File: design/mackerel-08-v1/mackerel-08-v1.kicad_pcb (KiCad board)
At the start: 4 copper layers, 160 x 99.1 mm, 40 parts, among them J1 Conn_02x20_Odd_Even, J2 DC_Jack, J3 Conn_02x10_Odd_Even, J4 Conn_02x10_Odd_Even, J5 Conn_01x06, J6 Conn_01x06, SW1 SW_Push, U1 MC68008, U10 XR68C681, U11 74HC595, U12 ATF22V10C, U13 74HC10, U14 ATF22V10C, U15 NE555P, U2 AS7C4096A, U3 AS7C4096A, U4 AS7C4096A, U5 AS7C4096A, U6 AS7C4096A, U7 AS7C4096A, U8 AS7C4096A, U9 SST39SF040, X1 CXO_DIP8, X2 CXO_DIP8

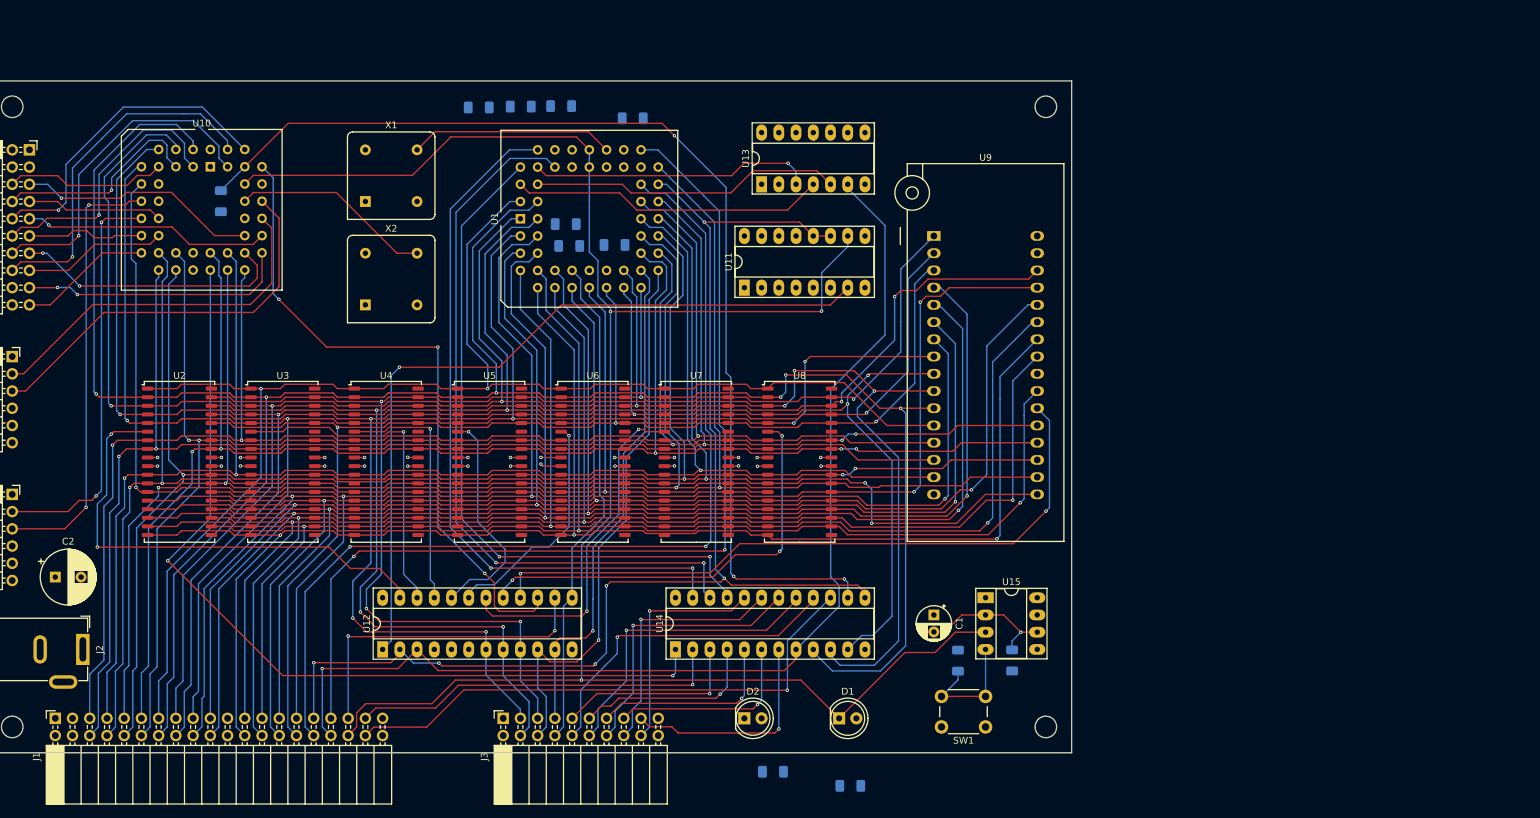
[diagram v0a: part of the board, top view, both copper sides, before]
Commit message: Add decoupling caps
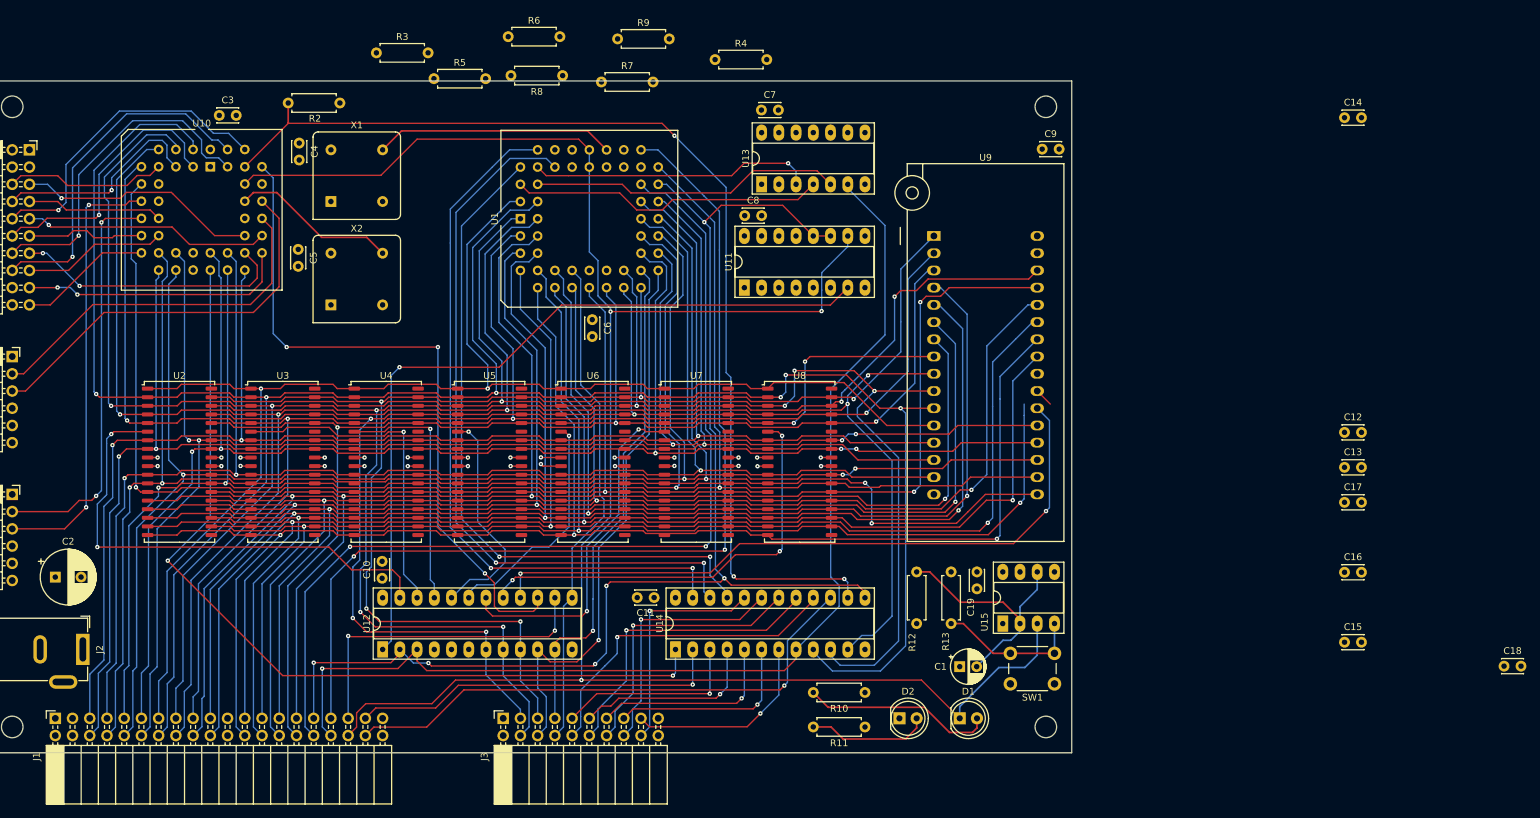
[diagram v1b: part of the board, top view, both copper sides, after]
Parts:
- added C10: C, Capacitor_THT:C_Disc_D3.0mm_W2.0mm_P2.50mm, F.Cu at (78.7, 93.6)
- added C11: C, Capacitor_THT:C_Disc_D3.0mm_W2.0mm_P2.50mm, F.Cu at (118.8, 96.5)
- added C12: C, Capacitor_THT:C_Disc_D3.0mm_W2.0mm_P2.50mm, F.Cu at (220.6, 72.1)
- added C13: C, Capacitor_THT:C_Disc_D3.0mm_W2.0mm_P2.50mm, F.Cu at (220.6, 77.3)
- added C14: C, Capacitor_THT:C_Disc_D3.0mm_W2.0mm_P2.50mm, F.Cu at (220.6, 25.7)
- added C15: C, Capacitor_THT:C_Disc_D3.0mm_W2.0mm_P2.50mm, F.Cu at (220.6, 103.1)
- added C16: C, Capacitor_THT:C_Disc_D3.0mm_W2.0mm_P2.50mm, F.Cu at (220.6, 92.8)
- added C17: C, Capacitor_THT:C_Disc_D3.0mm_W2.0mm_P2.50mm, F.Cu at (220.6, 82.5)
- added C18: C, Capacitor_THT:C_Disc_D3.0mm_W2.0mm_P2.50mm, F.Cu at (244.1, 106.6)
- added C19: C, Capacitor_THT:C_Disc_D3.0mm_W2.0mm_P2.50mm, F.Cu at (166.4, 92.7)
- added C3: C, Capacitor_THT:C_Disc_D3.0mm_W2.0mm_P2.50mm, F.Cu at (54.7, 25.4)
- added C4: C, Capacitor_THT:C_Disc_D3.0mm_W2.0mm_P2.50mm, F.Cu at (66.4, 29.5)
- added C5: C, Capacitor_THT:C_Disc_D3.0mm_W2.0mm_P2.50mm, F.Cu at (66.3, 45.2)
- added C6: C, Capacitor_THT:C_Disc_D3.0mm_W2.0mm_P2.50mm, F.Cu at (109.7, 55.5)
- added C7: C, Capacitor_THT:C_Disc_D3.0mm_W2.0mm_P2.50mm, F.Cu at (134.6, 24.6)
- added C8: C, Capacitor_THT:C_Disc_D3.0mm_W2.0mm_P2.50mm, F.Cu at (132.1, 40.2)
- added C9: C, Capacitor_THT:C_Disc_D3.0mm_W2.0mm_P2.50mm, F.Cu at (176.0, 30.4)
- R10, R11, R12, R13, R2, R3, R4, R5, R6, R7, R8, R9: footprint Resistor_SMD:R_1206_3216Metric_Pad1.30x1.75mm_HandSolder -> Resistor_THT:R_Axial_DIN0207_L6.3mm_D2.5mm_P7.62mm_Horizontal; moved to F.Cu
- moved R4 34.9 mm to (127.8, 17.2), turned to 0 degrees
- moved R6 34.5 mm to (97.3, 13.8), turned to 0 degrees
- moved R9 28.4 mm to (113.4, 14.1), turned to 0 degrees
- moved D2 22.9 mm to (154.9, 114.3)
- moved R12 19.2 mm to (157.5, 92.7)
- moved D1 17.8 mm to (163.8, 114.3)
- moved R2 17.6 mm to (64.8, 23.6), turned to 0 degrees
- moved R3 17.1 mm to (77.8, 16.2), turned to 0 degrees
- moved R11 15.1 mm to (149.9, 115.6), turned to 180 degrees
- moved R10 13.9 mm to (149.9, 110.5), turned to 180 degrees
- moved R5 13.4 mm to (86.3, 20.0), turned to 0 degrees
- moved R13 13.1 mm to (162.6, 92.7)
- moved SW1 12.0 mm to (177.8, 109.2)
- moved C1 8.52 mm to (163.8, 106.7), turned to 0 degrees
- moved R7 7.08 mm to (111.0, 20.5), turned to 0 degrees
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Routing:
- net Net-(D1-Pad2): track 0.00 -> 28.3 mm
- net Net-(D2-Pad2): track 0.00 -> 18.1 mm
- net Net-(C1-Pad2): track 20.5 -> 37.1 mm, vias 1 -> 0
- net //RESET: track 285.7 -> 297.3 mm
- net /CLK_CPU: track 30.1 -> 35.3 mm
- net /CLK_DUART: track 29.6 -> 24.5 mm
- net //IRQ7: track 33.2 -> 29.5 mm
- net //DUART0: track 97.0 -> 100.4 mm
- net Net-(R13-Pad2): track 18.2 -> 21.6 mm
- net //AS: track 186.8 -> 188.8 mm
- net //IACK1: track 159.8 -> 157.8 mm
- net //RAM0: track 71.5 -> 72.5 mm
- net //IACK: track 162.2 -> 163.2 mm
- net /IP5: track 51.9 -> 51.2 mm
- net //IACK2: track 81.3 -> 80.6 mm

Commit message: Rough layout of Mackerel-08 Rev1 PCB
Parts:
- added C20: C_Polarized_US, Capacitor_THT:CP_Radial_Tantal_D4.5mm_P5.00mm, F.Cu at (-123.8, 35.8)
- added C21: C_Polarized_US, Capacitor_THT:CP_Radial_Tantal_D4.5mm_P5.00mm, F.Cu at (-115.3, 44.3)
- added C22: C_Polarized_US, Capacitor_THT:CP_Radial_Tantal_D4.5mm_P5.00mm, F.Cu at (-75.1, 40.0)
- added C23: C_Polarized_US, Capacitor_THT:CP_Radial_Tantal_D4.5mm_P5.00mm, F.Cu at (-66.6, 40.0)
- added C24: C_Polarized_US, Capacitor_THT:CP_Radial_Tantal_D4.5mm_P5.00mm, F.Cu at (-115.3, 35.8)
- added C25: C_Polarized_US, Capacitor_THT:CP_Radial_Tantal_D4.5mm_P5.00mm, F.Cu at (-123.8, 44.3)
- added C26: C_Polarized_US, Capacitor_THT:CP_Radial_Tantal_D4.5mm_P5.00mm, F.Cu at (-66.6, 48.5)
- added C27: C_Polarized_US, Capacitor_THT:CP_Radial_Tantal_D4.5mm_P5.00mm, F.Cu at (-75.1, 48.5)
- added D3: LED, LED_THT:LED_D5.0mm, F.Cu at (-59.3, 198.7)
- added H1: MountingHole, MountingHole:MountingHole_3.7mm_Pad_Via, F.Cu at (26.0, 26.0)
- added H2: MountingHole, MountingHole:MountingHole_3.7mm_Pad_Via, F.Cu at (194.0, 26.0)
- added H3: MountingHole, MountingHole:MountingHole_3.7mm_Pad_Via, F.Cu at (26.0, 134.0)
- added H4: MountingHole, MountingHole:MountingHole_3.7mm_Pad_Via, F.Cu at (194.0, 134.0)
- added R1: R, Resistor_THT:R_Axial_DIN0207_L6.3mm_D2.5mm_P7.62mm_Horizontal, F.Cu at (-71.0, 197.0)
- added R14: R, Resistor_THT:R_Axial_DIN0207_L6.3mm_D2.5mm_P7.62mm_Horizontal, F.Cu at (-156.4, 90.8)
- added R15: R, Resistor_THT:R_Axial_DIN0207_L6.3mm_D2.5mm_P7.62mm_Horizontal, F.Cu at (-156.4, 86.8)
- added SW2: SW_SPDT, herring:SW_Mini_Toggle, F.Cu at (34.3, 35.3)
- added U16: MAX3232, Package_DIP:DIP-16_W7.62mm, F.Cu at (128.0, 45.0)
- J1: value Conn_02x20_Odd_Even -> Conn_01x08; footprint Connector_PinSocket_2.54mm:PinSocket_2x20_P2.54mm_Horizontal -> Connector_PinSocket_2.54mm:PinSocket_1x08_P2.54mm_Vertical
- J3, J4: value Conn_02x10_Odd_Even -> Conn_02x20_Counter_Clockwise; footprint Connector_PinSocket_2.54mm:PinSocket_2x10_P2.54mm_Horizontal -> Connector_IDC:IDC-Header_2x20_P2.54mm_Vertical
- J5, J6: value Conn_01x06 -> DB9_Male_MountingHoles; footprint Connector_PinSocket_2.54mm:PinSocket_1x06_P2.54mm_Horizontal -> Connector_Dsub:DSUB-9_Male_Horizontal_P2.77x2.84mm_EdgePinOffset7.70mm_Housed_MountingHolesOffset9.12mm
- U11: footprint Package_DIP:DIP-16_W7.62mm_Socket_LongPads -> Package_DIP:DIP-16_W7.62mm
- U12, U14: footprint Package_DIP:DIP-24_W7.62mm_Socket_LongPads -> Package_DIP:DIP-24_W7.62mm
- U13: value 74HC10 -> MAX3232; footprint Package_DIP:DIP-14_W7.62mm_Socket_LongPads -> Package_DIP:DIP-16_W7.62mm
- U15: footprint Package_DIP:DIP-8_W7.62mm_Socket_LongPads -> Package_DIP:DIP-8_W7.62mm
- U2, U3, U4, U5, U6, U7, U8: value AS7C4096A -> AS6C4008-55PCN; footprint Package_SO:SOJ-36_10.16x23.49mm_P1.27mm -> Package_DIP:DIP-32_W15.24mm
- U9: footprint Socket:DIP_Socket-32_W11.9_W12.7_W15.24_W17.78_W18.5_3M_232-1285-00-0602J -> Package_DIP:DIP-32_W15.24mm
- moved C14 372.3 mm to (-133.2, 141.7)
- moved C18 367.4 mm to (-121.9, 137.7)
- moved C12 354.5 mm to (-127.1, 141.7)
- moved C15 350.2 mm to (-127.1, 145.3)
- moved C17 346.9 mm to (-122.5, 134.1)
- moved C16 339.9 mm to (-116.8, 134.1)
- moved C13 330.2 mm to (-106.1, 126.0)
- moved R7 319.5 mm to (-161.8, 186.8)
- moved C9 304.3 mm to (-111.7, 129.6)
- moved C8 293.8 mm to (-137.8, 156.0)
- moved R5 290.1 mm to (-151.0, 186.8)
- moved C7 285.7 mm to (-127.6, 138.2)
- moved C1 275.0 mm to (-89.1, -1.17)
- moved C19 275.0 mm to (-86.6, -15.1)
- moved R10 275.0 mm to (-103.1, 2.64)
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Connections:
- net /BOOT renamed BOOT
- net /CLK_CPU renamed CLK_CPU
- net /CLK_DUART renamed Net-(U10-Pad36)
- net //IPL0 renamed /IPL0
- net //IPL1 renamed /IPL1
- net //IPL2 renamed /IPL2
- net //ROM0 renamed /ROM0
- D1 pad 1: //RESET -> /RESET
- J1 pad 2: +5V -> unconnected-(J1-Pad2)
- J1 pad 4: GND -> SPI_CLK
- J1 pad 5: /D0 -> SPI_DO
- J1 pad 6: /D1 -> SPI_DI
- J1 pad 7: /D2 -> SPI_CS0
- J1 pad 8: /D3 -> SD_CD
- J3 pad 1: +5V -> unconnected-(J3-Pad1)
- J3 pad 10: //IACK3 -> unconnected-(J3-Pad10)
- J3 pad 11: //IRQ4 -> unconnected-(J3-Pad11)
- J3 pad 12: //IACK4 -> unconnected-(J3-Pad12)
- J3 pad 13: //IRQ5 -> unconnected-(J3-Pad13)
- J3 pad 14: //IACK5 -> unconnected-(J3-Pad14)
- J3 pad 15: //IRQ6 -> unconnected-(J3-Pad15)
- J3 pad 16: //IACK6 -> unconnected-(J3-Pad16)
- J3 pad 17: //IRQ7 -> unconnected-(J3-Pad17)
- J3 pad 18: //IACK7 -> unconnected-(J3-Pad18)
- J3 pad 19: GND -> unconnected-(J3-Pad19)
- J3 pad 2: +5V -> unconnected-(J3-Pad2)
- J3 pad 20: GND -> unconnected-(J3-Pad20)
- J3 pad 3: /A16 -> unconnected-(J3-Pad3)
- J3 pad 4: /A17 -> unconnected-(J3-Pad4)
- J3 pad 5: /A18 -> unconnected-(J3-Pad5)
- J3 pad 6: /A19 -> unconnected-(J3-Pad6)
- J3 pad 7: /A20 -> unconnected-(J3-Pad7)
- J3 pad 8: /A21 -> unconnected-(J3-Pad8)
- J3 pad 9: //IRQ3 -> unconnected-(J3-Pad9)
- J4 pad 1: +5V -> unconnected-(J4-Pad1)
- J4 pad 10: /IP2 -> unconnected-(J4-Pad10)
- J4 pad 11: /OP3 -> unconnected-(J4-Pad11)
- J4 pad 12: /IP3 -> unconnected-(J4-Pad12)
- J4 pad 13: /OP4 -> unconnected-(J4-Pad13)
- J4 pad 14: /IP4 -> unconnected-(J4-Pad14)
- J4 pad 15: /OP5 -> unconnected-(J4-Pad15)
- J4 pad 16: /IP5 -> unconnected-(J4-Pad16)
- J4 pad 17: /OP6 -> unconnected-(J4-Pad17)
- J4 pad 18: GND -> unconnected-(J4-Pad18)
- J4 pad 19: /OP7 -> unconnected-(J4-Pad19)
- J4 pad 2: +5V -> unconnected-(J4-Pad2)
- J4 pad 20: GND -> unconnected-(J4-Pad20)
- J4 pad 3: GND -> unconnected-(J4-Pad3)
- J4 pad 4: GND -> unconnected-(J4-Pad4)
- J4 pad 5: /OP0 -> unconnected-(J4-Pad5)
- J4 pad 6: /IP0 -> unconnected-(J4-Pad6)
- J4 pad 7: /OP1 -> unconnected-(J4-Pad7)
- J4 pad 8: /IP1 -> unconnected-(J4-Pad8)
- J4 pad 9: /OP2 -> unconnected-(J4-Pad9)
- J5 pad 5: unconnected-(J5-Pad5) -> GND
- J5 pad 6: GND -> unconnected-(J5-Pad6)
- J6 pad 5: unconnected-(J6-Pad5) -> GND
- J6 pad 6: GND -> unconnected-(J6-Pad6)
- R2 pad 1: //IACK1 -> /IACK_DUART
- U1 pad 1: /A2 -> A2
- U1 pad 10: /A11 -> A11
- U1 pad 11: /A12 -> A12
- U1 pad 12: /A13 -> A13
- U1 pad 13: /A21 -> A21
- U1 pad 14: /A14 -> A14
- U1 pad 16: /A15 -> A15
- U1 pad 18: /A16 -> A16
- U1 pad 19: /A17 -> A17
- U1 pad 2: /A3 -> A3
- U1 pad 20: /A18 -> A18
- U1 pad 21: /A19 -> A19
- U1 pad 22: /A20 -> A20
- U1 pad 23: /D7 -> D7
- U1 pad 24: /D6 -> D6
- U1 pad 25: /D5 -> D5
- U1 pad 26: /D4 -> D4
- U1 pad 27: /D3 -> D3
- U1 pad 28: /D2 -> D2
- U1 pad 29: /D1 -> D1
- U1 pad 3: /A4 -> A4
- U1 pad 30: /D0 -> D0
- U1 pad 31: //AS -> /AS
- U1 pad 32: //DS -> /DS
- U1 pad 33: //RW -> /RW
- U1 pad 34: //DTACK -> /DTACK_CPU
- U1 pad 4: /A5 -> A5
- U1 pad 40: //RESET -> /RESET
- U1 pad 41: //RESET -> /RESET
- U1 pad 48: Net-(U1-Pad48) -> FC2
- U1 pad 49: Net-(U1-Pad49) -> FC1
- U1 pad 5: /A6 -> A6
- U1 pad 50: Net-(U1-Pad50) -> FC0
- U1 pad 51: /A0 -> A0
- U1 pad 52: /A1 -> A1
- U1 pad 6: /A7 -> A7
- U1 pad 7: /A8 -> A8
- U1 pad 8: /A9 -> A9
- U1 pad 9: /A10 -> A10
- U10 pad 11: Net-(J6-Pad3) -> RXB
- U10 pad 13: Net-(J6-Pad2) -> TXB
- U10 pad 14: /OP1 -> /RTSB
- U10 pad 15: /OP3 -> SPI_CLK
- U10 pad 16: /OP5 -> SPI_CS1
- U10 pad 17: /OP7 -> LED_U0
- U10 pad 18: /D1 -> D1
- U10 pad 19: /D3 -> D3
- U10 pad 2: /A1 -> A1
- U10 pad 20: /D5 -> D5
- U10 pad 21: /D7 -> D7
- U10 pad 24: //IRQ1 -> /INT_DUART
- U10 pad 25: /D6 -> D6
- U10 pad 26: /D4 -> D4
- U10 pad 27: /D2 -> D2
- U10 pad 28: /D0 -> D0
- U10 pad 29: /OP6 -> SPI_CS2
- U10 pad 3: /IP3 -> SPI_DO
- U10 pad 30: /OP4 -> SPI_CS0
- U10 pad 31: /OP2 -> SPI_DI
- U10 pad 32: /OP0 -> /RTSA
- U10 pad 33: Net-(J5-Pad2) -> TXA
- U10 pad 35: Net-(J5-Pad3) -> RXA
- U10 pad 38: //RESET -> /RESET
- U10 pad 39: //DUART0 -> /DUART
- U10 pad 4: /A2 -> A2
- U10 pad 40: /IP2 -> SD_CD
- U10 pad 41: //IACK1 -> /IACK_DUART
- U10 pad 42: /IP5 -> Net-(U10-Pad42)
- U10 pad 43: /IP4 -> Net-(U10-Pad43)
- U10 pad 5: /IP1 -> /CTSB
- U10 pad 6: /A3 -> A3
- U10 pad 7: /A4 -> A4
- U10 pad 8: /IP0 -> /CTSA
- U10 pad 9: //RW -> /RW
- U11 pad 10: //RESET -> /RESET
- U11 pad 11: //AS -> /AS
- U11 pad 12: //AS -> /AS
- U12 pad 10: /A19 -> A19
- U12 pad 11: /A20 -> A20
- U12 pad 13: /A21 -> A21
- U12 pad 17: //RAM6 -> /RAM6
- U12 pad 18: //RAM5 -> /RAM5
- U12 pad 19: //RAM4 -> /RAM4
- U12 pad 2: //AS -> /AS
- U12 pad 20: //RAM3 -> /RAM3
- U12 pad 21: //RAM2 -> /RAM2
- U12 pad 22: //RAM1 -> /RAM1
- U12 pad 23: //RAM0 -> /RAM0
- U12 pad 7: /A16 -> A16
- U12 pad 8: /A17 -> A17
- U12 pad 9: /A18 -> A18
- U13 pad 1: GND -> Net-(C20-Pad1)
- U13 pad 10: GND -> /RTSA
- U13 pad 11: GND -> TXA
- U13 pad 12: unconnected-(U13-Pad12) -> RXA
- U13 pad 13: GND -> Net-(J5-Pad2)
- U13 pad 14: +5V -> Net-(J5-Pad3)
- U13 pad 2: GND -> Net-(C24-Pad1)
- U13 pad 3: Net-(U1-Pad48) -> Net-(C20-Pad2)
- U13 pad 4: Net-(U1-Pad49) -> Net-(C22-Pad1)
- U13 pad 5: Net-(U1-Pad50) -> Net-(C22-Pad2)
- U13 pad 6: //IACK -> Net-(C25-Pad2)
- U13 pad 7: GND -> Net-(J5-Pad7)
- U13 pad 8: unconnected-(U13-Pad8) -> Net-(J5-Pad8)
- U13 pad 9: GND -> /CTSA
- U14 pad 10: /A2 -> A2
- U14 pad 11: /A3 -> A3
- U14 pad 13: //AS -> /AS
- U14 pad 16: //IACK3 -> unconnected-(U14-Pad16)
- U14 pad 17: //IACK4 -> unconnected-(U14-Pad17)
- U14 pad 18: //IACK5 -> unconnected-(U14-Pad18)
- U14 pad 19: //IACK6 -> //IACK
- U14 pad 20: //IACK7 -> unconnected-(U14-Pad20)
- U14 pad 3: //IRQ3 -> unconnected-(U14-Pad3)
- U14 pad 4: //IRQ4 -> FC0
- U14 pad 5: //IRQ5 -> FC1
- U14 pad 6: //IRQ6 -> FC2
- U14 pad 7: //IRQ7 -> unconnected-(U14-Pad7)
- U14 pad 8: //IACK -> unconnected-(U14-Pad8)
- U14 pad 9: /A1 -> A1
- U15 pad 3: //RESET -> /RESET
- U2 pad 1: /A0 -> A18
- U2 pad 10: GND -> A2
- U2 pad 11: /D2 -> A1
- U2 pad 12: /D3 -> A0
- U2 pad 13: //RW -> D0
- U2 pad 14: /A5 -> D1
- U2 pad 15: /A6 -> D2
- U2 pad 16: /A7 -> GND
- U2 pad 17: /A8 -> D3
- U2 pad 18: /A9 -> D4
- U2 pad 19: unconnected-(U2-Pad19) -> D5
- U2 pad 2: /A1 -> A16
- U2 pad 20: /A10 -> D6
- U2 pad 21: /A11 -> D7
- U2 pad 22: /A12 -> /RAM0
- U2 pad 23: /A13 -> A10
- U2 pad 24: /A14 -> GND
- U2 pad 25: /D4 -> A11
- U2 pad 26: /D5 -> A9
- U2 pad 27: +5V -> A8
- U2 pad 28: GND -> A13
- U2 pad 29: /D6 -> /RW
- U2 pad 3: /A2 -> A14
- U2 pad 30: /D7 -> A17
- U2 pad 31: GND -> A15
- U2 pad 32: /A15 -> +5V
- U2 pad 4: /A3 -> A12
- U2 pad 5: /A4 -> A7
- U2 pad 6: //RAM0 -> A6
- U2 pad 7: /D0 -> A5
- U2 pad 8: /D1 -> A4
- U2 pad 9: +5V -> A3
- U3 pad 1: /A0 -> A18
- U3 pad 10: GND -> A2
- U3 pad 11: /D2 -> A1
- U3 pad 12: /D3 -> A0
- U3 pad 13: //RW -> D0
- U3 pad 14: /A5 -> D1
- U3 pad 15: /A6 -> D2
- U3 pad 16: /A7 -> GND
- U3 pad 17: /A8 -> D3
- U3 pad 18: /A9 -> D4
- U3 pad 19: unconnected-(U3-Pad19) -> D5
- U3 pad 2: /A1 -> A16
- U3 pad 20: /A10 -> D6
- U3 pad 21: /A11 -> D7
- U3 pad 22: /A12 -> /RAM1
- U3 pad 23: /A13 -> A10
- U3 pad 24: /A14 -> GND
- U3 pad 25: /D4 -> A11
- U3 pad 26: /D5 -> A9
- U3 pad 27: +5V -> A8
- U3 pad 28: GND -> A13
- U3 pad 29: /D6 -> /RW
- U3 pad 3: /A2 -> A14
- U3 pad 30: /D7 -> A17
- U3 pad 31: GND -> A15
- U3 pad 32: /A15 -> +5V
- U3 pad 4: /A3 -> A12
- U3 pad 5: /A4 -> A7
- U3 pad 6: //RAM1 -> A6
- U3 pad 7: /D0 -> A5
- U3 pad 8: /D1 -> A4
- U3 pad 9: +5V -> A3
- U4 pad 1: /A0 -> A18
- U4 pad 10: GND -> A2
- U4 pad 11: /D2 -> A1
- U4 pad 12: /D3 -> A0
- U4 pad 13: //RW -> D0
- U4 pad 14: /A5 -> D1
- U4 pad 15: /A6 -> D2
- U4 pad 16: /A7 -> GND
- U4 pad 17: /A8 -> D3
- U4 pad 18: /A9 -> D4
- U4 pad 19: unconnected-(U4-Pad19) -> D5
- U4 pad 2: /A1 -> A16
- U4 pad 20: /A10 -> D6
- U4 pad 21: /A11 -> D7
- U4 pad 22: /A12 -> /RAM2
- U4 pad 23: /A13 -> A10
- U4 pad 24: /A14 -> GND
- U4 pad 25: /D4 -> A11
- U4 pad 26: /D5 -> A9
- U4 pad 27: +5V -> A8
- U4 pad 28: GND -> A13
- U4 pad 29: /D6 -> /RW
- U4 pad 3: /A2 -> A14
- U4 pad 30: /D7 -> A17
- U4 pad 31: GND -> A15
- U4 pad 32: /A15 -> +5V
- U4 pad 4: /A3 -> A12
- U4 pad 5: /A4 -> A7
- U4 pad 6: //RAM2 -> A6
- U4 pad 7: /D0 -> A5
- U4 pad 8: /D1 -> A4
- U4 pad 9: +5V -> A3
- U5 pad 1: /A0 -> A18
- U5 pad 10: GND -> A2
- U5 pad 11: /D2 -> A1
- U5 pad 12: /D3 -> A0
- U5 pad 13: //RW -> D0
- U5 pad 14: /A5 -> D1
- U5 pad 15: /A6 -> D2
- U5 pad 16: /A7 -> GND
- U5 pad 17: /A8 -> D3
- U5 pad 18: /A9 -> D4
- U5 pad 19: unconnected-(U5-Pad19) -> D5
- U5 pad 2: /A1 -> A16
- U5 pad 20: /A10 -> D6
- U5 pad 21: /A11 -> D7
- U5 pad 22: /A12 -> /RAM3
- U5 pad 23: /A13 -> A10
- U5 pad 24: /A14 -> GND
- U5 pad 25: /D4 -> A11
- U5 pad 26: /D5 -> A9
- U5 pad 27: +5V -> A8
- U5 pad 28: GND -> A13
- U5 pad 29: /D6 -> /RW
- U5 pad 3: /A2 -> A14
- U5 pad 30: /D7 -> A17
- U5 pad 31: GND -> A15
- U5 pad 32: /A15 -> +5V
- U5 pad 4: /A3 -> A12
- U5 pad 5: /A4 -> A7
- U5 pad 6: //RAM3 -> A6
- U5 pad 7: /D0 -> A5
- U5 pad 8: /D1 -> A4
- U5 pad 9: +5V -> A3
- U6 pad 1: /A0 -> A18
- U6 pad 10: GND -> A2
- U6 pad 11: /D2 -> A1
- U6 pad 12: /D3 -> A0
- U6 pad 13: //RW -> D0
- U6 pad 14: /A5 -> D1
- U6 pad 15: /A6 -> D2
- U6 pad 16: /A7 -> GND
- U6 pad 17: /A8 -> D3
- U6 pad 18: /A9 -> D4
- U6 pad 19: unconnected-(U6-Pad19) -> D5
- U6 pad 2: /A1 -> A16
- U6 pad 20: /A10 -> D6
- U6 pad 21: /A11 -> D7
- U6 pad 22: /A12 -> /RAM5
- U6 pad 23: /A13 -> A10
- U6 pad 24: /A14 -> GND
- U6 pad 25: /D4 -> A11
- U6 pad 26: /D5 -> A9
- U6 pad 27: +5V -> A8
- U6 pad 28: GND -> A13
- U6 pad 29: /D6 -> /RW
- U6 pad 3: /A2 -> A14
- U6 pad 30: /D7 -> A17
- U6 pad 31: GND -> A15
- U6 pad 32: /A15 -> +5V
- U6 pad 4: /A3 -> A12
- U6 pad 5: /A4 -> A7
- U6 pad 6: //RAM4 -> A6
- U6 pad 7: /D0 -> A5
- U6 pad 8: /D1 -> A4
- U6 pad 9: +5V -> A3
- U7 pad 1: /A0 -> A18
- U7 pad 10: GND -> A2
- U7 pad 11: /D2 -> A1
- U7 pad 12: /D3 -> A0
- U7 pad 13: //RW -> D0
- U7 pad 14: /A5 -> D1
- U7 pad 15: /A6 -> D2
- U7 pad 16: /A7 -> GND
- U7 pad 17: /A8 -> D3
- U7 pad 18: /A9 -> D4
- U7 pad 19: unconnected-(U7-Pad19) -> D5
- U7 pad 2: /A1 -> A16
- U7 pad 20: /A10 -> D6
- U7 pad 21: /A11 -> D7
- U7 pad 22: /A12 -> /RAM4
- U7 pad 23: /A13 -> A10
- U7 pad 24: /A14 -> GND
- U7 pad 25: /D4 -> A11
- U7 pad 26: /D5 -> A9
- U7 pad 27: +5V -> A8
- U7 pad 28: GND -> A13
- U7 pad 29: /D6 -> /RW
- U7 pad 3: /A2 -> A14
- U7 pad 30: /D7 -> A17
- U7 pad 31: GND -> A15
- U7 pad 32: /A15 -> +5V
- U7 pad 4: /A3 -> A12
- U7 pad 5: /A4 -> A7
- U7 pad 6: //RAM5 -> A6
- U7 pad 7: /D0 -> A5
- U7 pad 8: /D1 -> A4
- U7 pad 9: +5V -> A3
- U8 pad 1: /A0 -> A18
- U8 pad 10: GND -> A2
- U8 pad 11: /D2 -> A1
- U8 pad 12: /D3 -> A0
- U8 pad 13: //RW -> D0
- U8 pad 14: /A5 -> D1
- U8 pad 15: /A6 -> D2
- U8 pad 16: /A7 -> GND
- U8 pad 17: /A8 -> D3
- U8 pad 18: /A9 -> D4
- U8 pad 19: unconnected-(U8-Pad19) -> D5
- U8 pad 2: /A1 -> A16
- U8 pad 20: /A10 -> D6
- U8 pad 21: /A11 -> D7
- U8 pad 22: /A12 -> /RAM6
- U8 pad 23: /A13 -> A10
- U8 pad 24: /A14 -> GND
- U8 pad 25: /D4 -> A11
- U8 pad 26: /D5 -> A9
- U8 pad 27: +5V -> A8
- U8 pad 28: GND -> A13
- U8 pad 29: /D6 -> /RW
- U8 pad 3: /A2 -> A14
- U8 pad 30: /D7 -> A17
- U8 pad 31: GND -> A15
- U8 pad 32: /A15 -> +5V
- U8 pad 4: /A3 -> A12
- U8 pad 5: /A4 -> A7
- U8 pad 6: //RAM6 -> A6
- U8 pad 7: /D0 -> A5
- U8 pad 8: /D1 -> A4
- U8 pad 9: +5V -> A3
- U9 pad 1: /A18 -> A18
- U9 pad 10: /A2 -> A2
- U9 pad 11: /A1 -> A1
- U9 pad 12: /A0 -> A0
- U9 pad 13: /D0 -> D0
- U9 pad 14: /D1 -> D1
- U9 pad 15: /D2 -> D2
- U9 pad 16: GND -> Net-(U9-Pad16)
- U9 pad 17: /D3 -> D3
- U9 pad 18: /D4 -> D4
- U9 pad 19: /D5 -> D5
- U9 pad 2: /A16 -> A16
- U9 pad 20: /D6 -> D6
- U9 pad 21: /D7 -> D7
- U9 pad 23: /A10 -> A10
- U9 pad 24: GND -> Net-(U9-Pad16)
- U9 pad 25: /A11 -> A11
- U9 pad 26: /A9 -> A9
- U9 pad 27: /A8 -> A8
- U9 pad 28: /A13 -> A13
- U9 pad 29: /A14 -> A14
- U9 pad 3: /A15 -> A15
- U9 pad 30: /A17 -> A17
- U9 pad 4: /A12 -> A12
- U9 pad 5: /A7 -> A7
- U9 pad 6: /A6 -> A6
- U9 pad 7: /A5 -> A5
- U9 pad 8: /A4 -> A4
- U9 pad 9: /A3 -> A3
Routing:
- net /A1: track 328.3 -> 0.00 mm, vias 6 -> 0
- net /A2: track 315.7 -> 0.00 mm, vias 6 -> 0
- net /A3: track 299.6 -> 0.00 mm, vias 5 -> 0
- net //RESET: track 297.3 -> 0.00 mm, vias 3 -> 0
- net /D3: track 259.1 -> 0.00 mm, vias 5 -> 0
- net /A4: track 250.9 -> 0.00 mm, vias 5 -> 0
- net /D4: track 243.6 -> 0.00 mm, vias 3 -> 0
- net /D5: track 242.9 -> 0.00 mm, vias 4 -> 0
- net /A7: track 238.4 -> 0.00 mm, vias 3 -> 0
- net /D7: track 235.4 -> 0.00 mm, vias 5 -> 0
- net /D2: track 235.0 -> 0.00 mm, vias 3 -> 0
- net /D1: track 233.6 -> 0.00 mm, vias 3 -> 0
- net /D6: track 233.4 -> 0.00 mm, vias 5 -> 0
- net /A8: track 232.8 -> 0.00 mm, vias 3 -> 0
- net /A5: track 232.1 -> 0.00 mm, vias 3 -> 0
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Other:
- board size 160 x 99.1 mm -> 180 x 120 mm
- board text added: "5V"
- board text added: "CD"
- board text added: "CLK"
- board text added: "CS"
- board text added: "DI"
- board text added: "DO"
- board text added: "GND"
